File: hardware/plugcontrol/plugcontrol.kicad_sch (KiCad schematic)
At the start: 0 parts

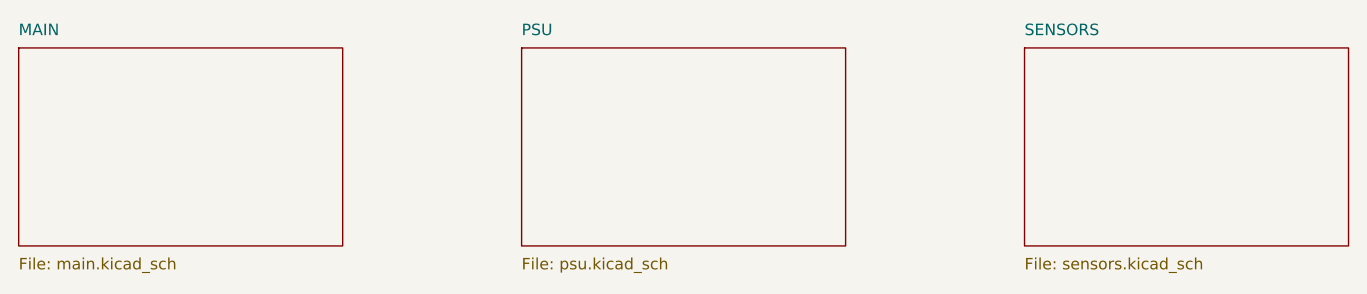
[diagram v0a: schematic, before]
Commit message: hardware: place parts for DryContact, PlugControl, SensorBuddy
Generate each board's schematic from a scripts/<board>.schgen.py manifest —
every part resolves to a real KiCad symbol + matching footprint + 3D model + LCSC.
Parts are PLACED, not wired (wire in eeschema; each sheet carries a pinout note).
make check-<board> = structure sound for all three:
- DryContact  (NEW): 49 components — STM32G0B1 + TCAN1044 + ULN2003 + 4x Omron
  G6K-2F-Y Form-C dry contacts; 29-bit CAN, UID auto-address. + BOM + handsolder.
- PlugControl (NEW KiCad project): 88 components — mcu/safety/actuation. A few
  generic stand-in symbols (TLV3202/74HC08/REF3330/TPS3823/SSR) pending swap;
  footprints/LCSC are correct.
- SensorBuddy (regenerated from placeholders): 81 components — ESP32-S3 + STM32G0B1
  + isolated ADM3260/ADS1115/OPA2376 probe front-end + NTC/1-Wire/floats.
Reuses the existing custom symbols in lib/symbols/sensorbuddy.kicad_sym.

Co-Authored-By: Claude Opus 4.8 (1M context) <noreply@anthropic.com>
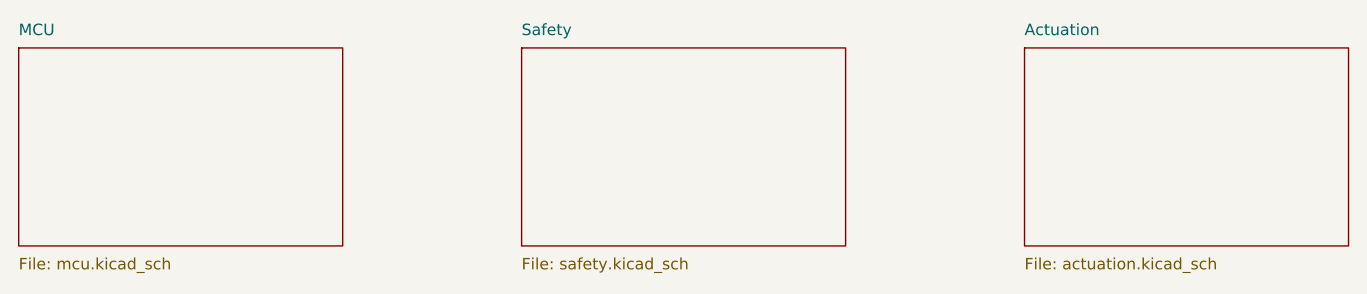
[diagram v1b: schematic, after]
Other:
- removed sheet MAIN
- removed sheet PSU
- removed sheet SENSORS
- added sheet Actuation (actuation.kicad_sch)
- added sheet MCU (mcu.kicad_sch)
- added sheet Safety (safety.kicad_sch)
- title: ReefVolt SensorBuddy — Main -> ReefVolt PlugControl — 2ch AC heater carrier
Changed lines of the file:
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@@
 	(paper "A3")
 	(title_block
-		(title "ReefVolt SensorBuddy — Main")
+		(title "ReefVolt PlugControl — 2ch AC heater carrier")
 		(date "2026-07-04")
 		(rev "0.1")
 		(company "blueAcro / ReefVolt")
-		(comment 1 "Aquarium sensor interface — CAN master of the SensorBuddy cluster")
-		(comment 2 "ESP32-S3 + STM32G0B1 + isolated pH/ORP + NTC + 1-Wire + floats")
+		(comment 1 "2-channel AC heater carrier with independent hardware safety interlock")
+		(comment 2 "STM32G0B1 + TCAN1044; 2x SSR + master G5LE relay; analog safety chain (REF3330/TLV3202/74HC74/74HC08/TPS3823)")
 	)
 	(sheet
@@
 		(stroke (width 0.1524) (type solid))
 		(fill (color 0 0 0 0.0000))
-		(property "Sheetname" "MAIN"
+		(property "Sheetname" "MCU"
 			(at 40.64 39.37 0)
 			(effects (font (size 1.27 1.27)) (justify left bottom))
 		)
-		(property "Sheetfile" "main.kicad_sch"
+		(property "Sheetfile" "mcu.kicad_sch"
 			(at 40.64 63.91 0)
 			(effects (font (size 1.27 1.27)) (justify left top))
@@
 		(stroke (width 0.1524) (type solid))
 		(fill (color 0 0 0 0.0000))
-		(property "Sheetname" "PSU"
+		(property "Sheetname" "Safety"
 			(at 96.52 39.37 0)
 			(effects (font (size 1.27 1.27)) (justify left bottom))
 		)
-		(property "Sheetfile" "psu.kicad_sch"
+		(property "Sheetfile" "safety.kicad_sch"
 			(at 96.52 63.91 0)
 			(effects (font (size 1.27 1.27)) (justify left top))
@@
 		(stroke (width 0.1524) (type solid))
 		(fill (color 0 0 0 0.0000))
-		(property "Sheetname" "SENSORS"
+		(property "Sheetname" "Actuation"
 			(at 152.40 39.37 0)
 			(effects (font (size 1.27 1.27)) (justify left bottom))
 		)
-		(property "Sheetfile" "sensors.kicad_sch"
+		(property "Sheetfile" "actuation.kicad_sch"
 			(at 152.40 63.91 0)
 			(effects (font (size 1.27 1.27)) (justify left top))
